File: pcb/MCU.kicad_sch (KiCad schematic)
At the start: 10 parts, among them U1 WeMos_S2_mini

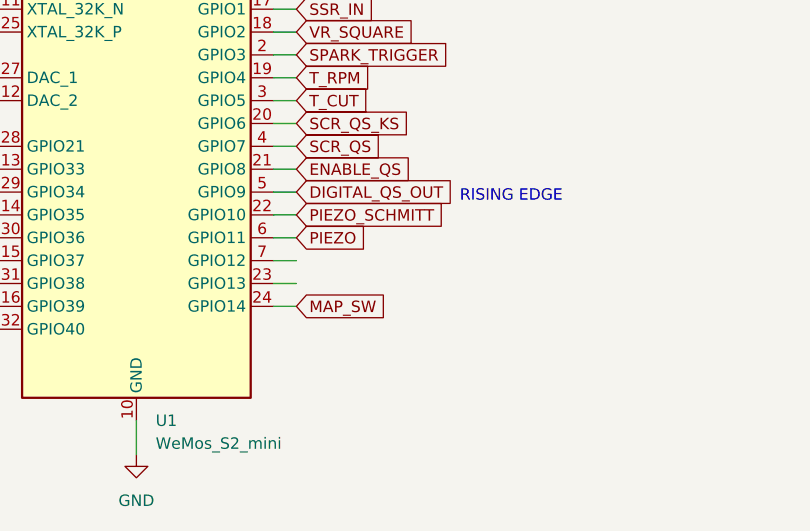
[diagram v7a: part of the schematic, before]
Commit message: enhanced spark detection circuit
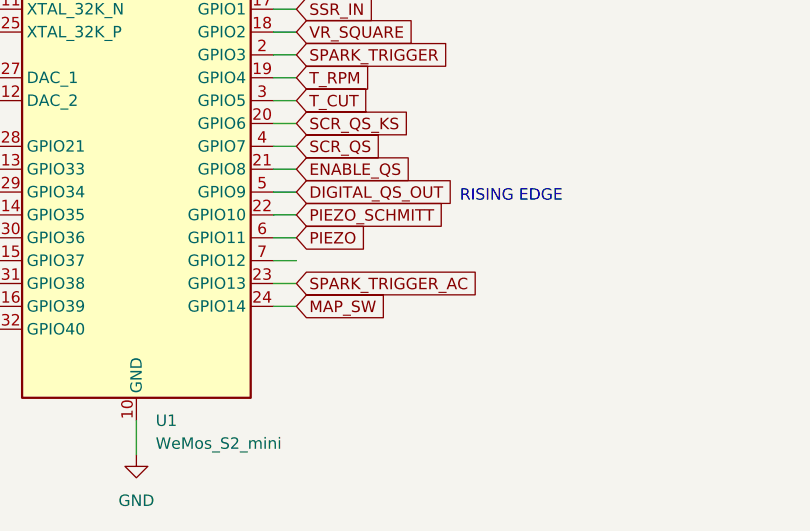
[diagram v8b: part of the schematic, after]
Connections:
- net SPARK_TRIGGER_AC: now reaches U1.23 (GPIO13)
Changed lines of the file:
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@@
+		)
+	)
+	(global_label "SPARK_TRIGGER_AC"
+		(shape input)
+		(at 106.68 82.55 0)
+		(fields_autoplaced yes)
+		(effects
+			(font
+				(size 1.27 1.27)
+			)
+			(justify left)
+		)
+		(property "Intersheetrefs" "${INTERSHEET_REFS}"
+			(at 127.8685 82.55 0)
+			(effects
+				(font
+					(size 1.27 1.27)
+				)
+				(justify left)
+				(hide yes)
+			)
 		)
 	)
